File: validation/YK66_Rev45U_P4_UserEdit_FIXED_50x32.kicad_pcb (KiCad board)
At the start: 2 copper layers, 50 x 32 mm, 13 parts, among them J1 PHOENIX_1711725_2P_5p08

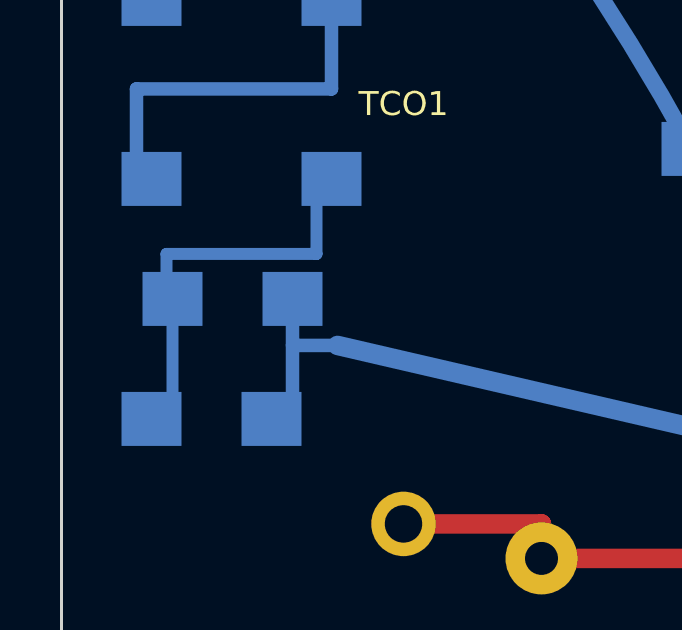
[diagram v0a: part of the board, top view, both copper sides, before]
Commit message: Replace 1206 LED with 3mm remote wired white LED through-hole solder pads
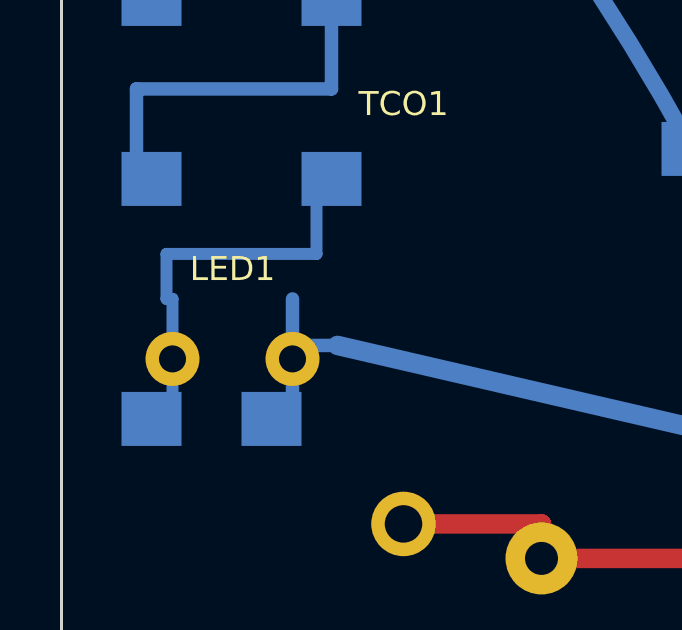
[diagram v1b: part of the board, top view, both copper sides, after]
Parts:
- LED1: value WHITE_1206_HI_EFF_TBD -> WHITE_LED_3MM_REMOTE_WIRED; footprint YK66:LED_1206_Bottom -> YK66:LED_3MM_Remote_Wired_PTH; moved to F.Cu
- moved LED1 2.00 mm to (5.70, 21.0)
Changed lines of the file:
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@@
 		(embedded_fonts no)
 	)
-	(footprint "YK66:LED_1206_Bottom"
-		(layer "B.Cu")
-		(at 5.7 19)
+	(footprint "YK66:LED_3MM_Remote_Wired_PTH"
+		(layer "F.Cu")
+		(at 5.7 21)
 		(property "Reference" "LED1"
 			(at 0 -3 0)
-			(layer "B.SilkS")
+			(layer "F.SilkS")
 			(effects
 				(font
@@
 					(thickness 0.12)
 				)
-				(justify mirror)
 			)
 		)
-		(property "Value" "WHITE_1206_HI_EFF_TBD"
+		(property "Value" "WHITE_LED_3MM_REMOTE_WIRED"
 			(at 0 3 0)
-			(layer "B.Fab")
+			(layer "F.Fab")
 			(effects
 				(font
@@
 					(thickness 0.1)
 				)
-				(justify mirror)
 			)
 		)
@@
 			)
 		)
-		(attr smd)
-		(fp_rect
-			(start -1.85 -0.9)
-			(end 1.85 0.9)
-			(stroke
-				(width 0.12)
-				(type default)
-			)
-			(fill no)
-			(layer "B.Fab")
-		)
-		(pad "1" smd rect
-			(at -2 0)
-			(size 2 1.8)
-			(layers "B.Cu" "B.Mask" "B.Paste")
-			(net 8 "/LED_A")
-			(pinfunction "1")
-			(pintype "passive")
-		)
-		(pad "2" smd rect
-			(at 2 0)
-			(size 2 1.8)
-			(layers "B.Cu" "B.Mask" "B.Paste")
-			(net 4 "/N")
-			(pinfunction "2")
-			(pintype "passive")
-		)
+		(attr through_hole)
+		(fp_circle
+            (center 0 0)
+            (end 1.5 0)
+            (stroke (width 0.12) (type default))
+            (fill no)
+            (layer "F.Fab")
+        )
+		(pad "1" thru_hole circle
+            (at -2 0)
+            (size 1.8 1.8)
+            (drill 0.9)
+            (layers "*.Cu" "*.Mask")
+            (net 8 "/LED_A")
+            (pinfunction "A")
+            (pintype "passive")
+        )
+		(pad "2" thru_hole circle
+            (at 2 0)
+            (size 1.8 1.8)
+            (drill 0.9)
+            (layers "*.Cu" "*.Mask")
+            (net 4 "/N")
+            (pinfunction "K")
+            (pintype "passive")
+        )
 		(embedded_fonts no)
 	)

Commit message: Fix dangling neutral track endpoint after remote wired LED footprint change
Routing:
- net /N: track 76.5 -> 74.9 mm
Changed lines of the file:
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@@
 	)
 	(segment
-		(start 7.7000 19.0000)
+		(start 7.7000 20.5500)
 		(end 7.7000 23.0000)
 		(width 0.450)

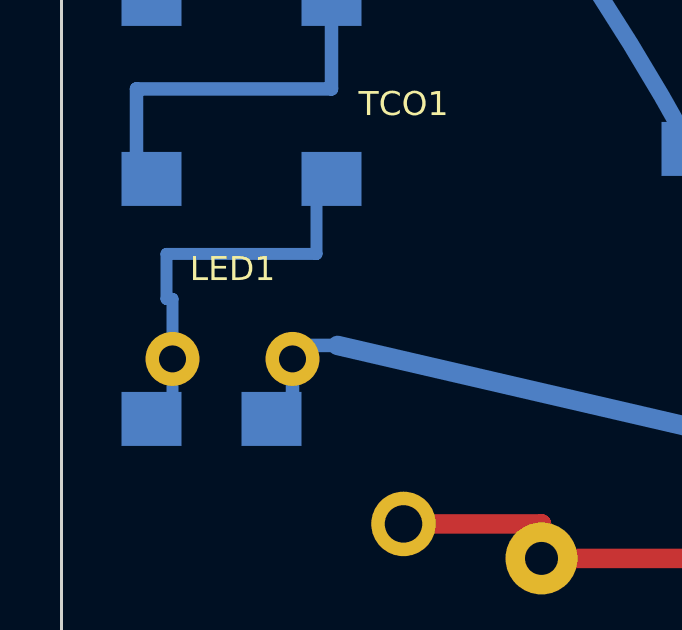
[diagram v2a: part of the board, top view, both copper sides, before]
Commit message: Restore 1206 SMD LED at safer relocated pads; remove remote wired LED
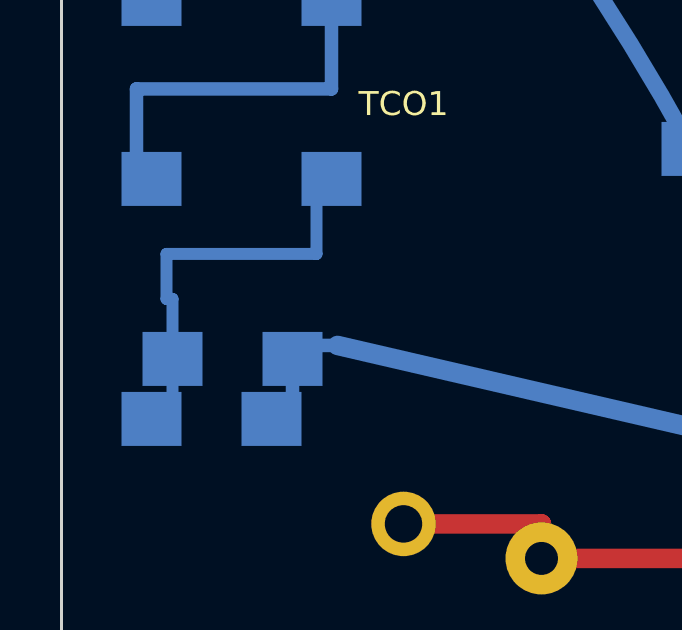
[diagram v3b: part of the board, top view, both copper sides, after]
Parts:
- LED1: value WHITE_LED_3MM_REMOTE_WIRED -> WHITE_1206_HI_EFF_TBD; footprint YK66:LED_3MM_Remote_Wired_PTH -> YK66:LED_1206_Bottom; moved to B.Cu
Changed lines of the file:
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@@
 		(embedded_fonts no)
 	)
-	(footprint "YK66:LED_3MM_Remote_Wired_PTH"
-		(layer "F.Cu")
+	(footprint "YK66:LED_1206_Bottom"
+		(layer "B.Cu")
 		(at 5.7 21)
 		(property "Reference" "LED1"
 			(at 0 -3 0)
-			(layer "F.SilkS")
+			(layer "B.SilkS")
 			(effects
 				(font
@@
 					(thickness 0.12)
 				)
+				(justify mirror)
 			)
 		)
-		(property "Value" "WHITE_LED_3MM_REMOTE_WIRED"
+		(property "Value" "WHITE_1206_HI_EFF_TBD"
 			(at 0 3 0)
-			(layer "F.Fab")
+			(layer "B.Fab")
 			(effects
 				(font
@@
 					(thickness 0.1)
 				)
+				(justify mirror)
 			)
 		)
@@
 			)
 		)
-		(attr through_hole)
-		(fp_circle
-            (center 0 0)
-            (end 1.5 0)
-            (stroke (width 0.12) (type default))
-            (fill no)
-            (layer "F.Fab")
-        )
-		(pad "1" thru_hole circle
-            (at -2 0)
-            (size 1.8 1.8)
-            (drill 0.9)
-            (layers "*.Cu" "*.Mask")
-            (net 8 "/LED_A")
-            (pinfunction "A")
-            (pintype "passive")
-        )
-		(pad "2" thru_hole circle
-            (at 2 0)
-            (size 1.8 1.8)
-            (drill 0.9)
-            (layers "*.Cu" "*.Mask")
-            (net 4 "/N")
-            (pinfunction "K")
-            (pintype "passive")
-        )
+		(attr smd)
+		(fp_rect
+			(start -1.85 -0.9)
+			(end 1.85 0.9)
+			(stroke
+				(width 0.12)
+				(type default)
+			)
+			(fill no)
+			(layer "B.Fab")
+		)
+		(pad "1" smd rect
+			(at -2 0)
+			(size 2 1.8)
+			(layers "B.Cu" "B.Mask" "B.Paste")
+			(net 8 "/LED_A")
+			(pinfunction "1")
+			(pintype "passive")
+		)
+		(pad "2" smd rect
+			(at 2 0)
+			(size 2 1.8)
+			(layers "B.Cu" "B.Mask" "B.Paste")
+			(net 4 "/N")
+			(pinfunction "2")
+			(pintype "passive")
+		)
 		(embedded_fonts no)
 	)

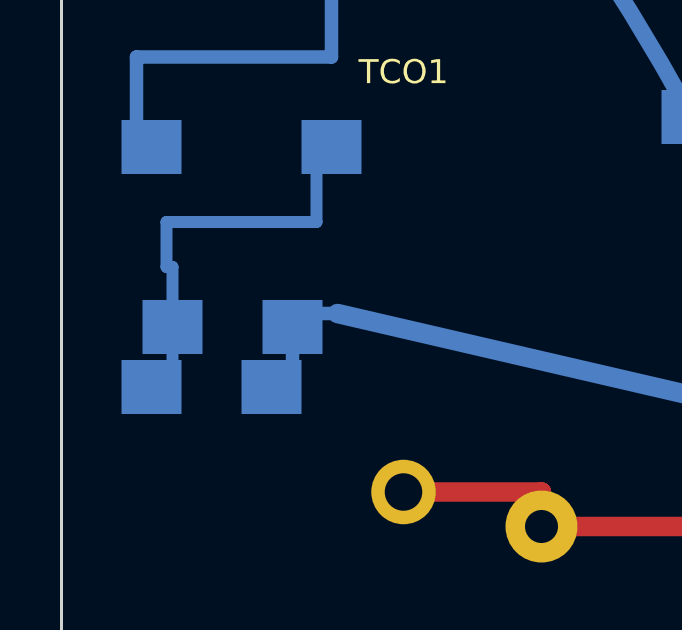
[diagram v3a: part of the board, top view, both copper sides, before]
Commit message: Increase D1-to-LED1 clearance by moving 1206 LED 0.8mm upward without changing tracks
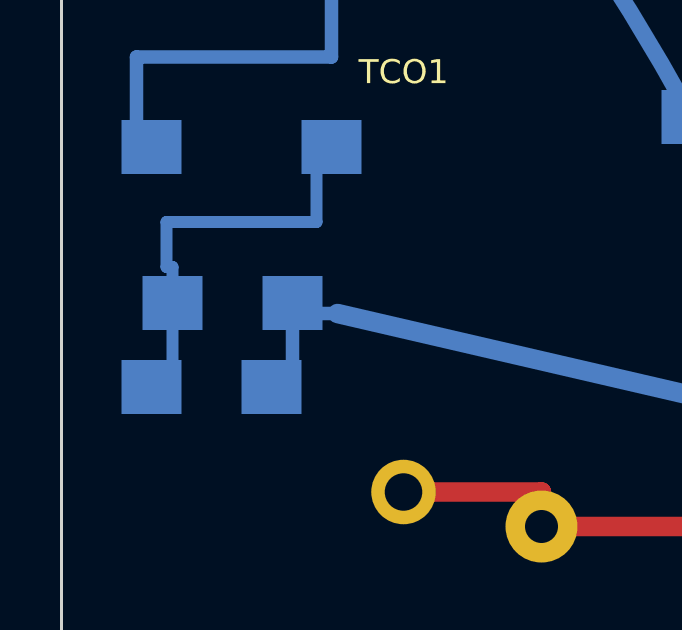
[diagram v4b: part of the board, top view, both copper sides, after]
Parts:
- moved LED1 0.80 mm to (5.70, 20.2)
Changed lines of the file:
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@@
 	(footprint "YK66:LED_1206_Bottom"
 		(layer "B.Cu")
-		(at 5.7 21)
+		(at 5.7 20.2)
 		(property "Reference" "LED1"
 			(at 0 -3 0)
